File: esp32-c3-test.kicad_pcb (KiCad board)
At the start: 2 copper layers, 40 x 40 mm, 31 parts, among them J1 Conn_01x03, J2 Conn_01x02, J3 Conn_01x01, J4 Conn_01x02, J5 Conn_01x02, J6 Conn_01x02, J9 USB_B_Micro, Q1 DTC143E, Q2 DTC143E, Q3 DTC143E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

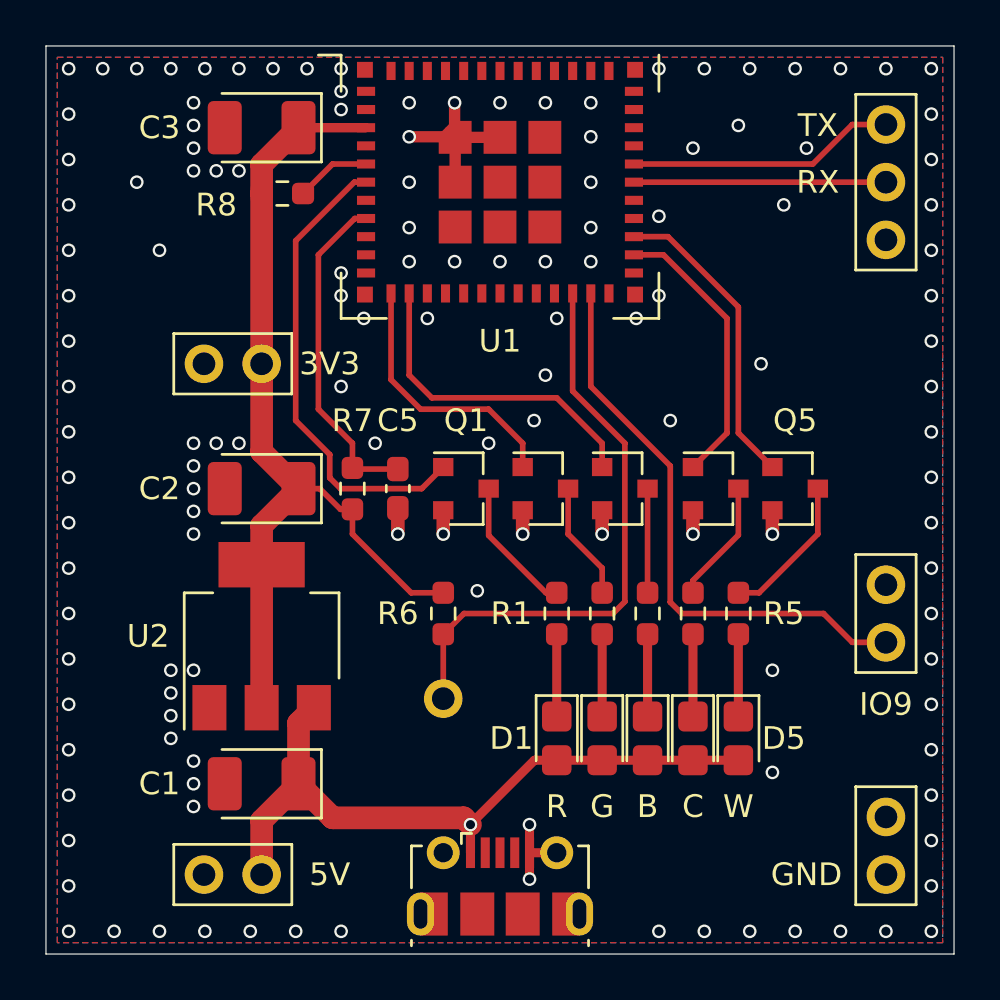
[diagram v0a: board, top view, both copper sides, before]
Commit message: 1. change c5 to c4 2. modify silkscreen of esp32-c3-mini-1 footprint to avoid via 3. move a few vias
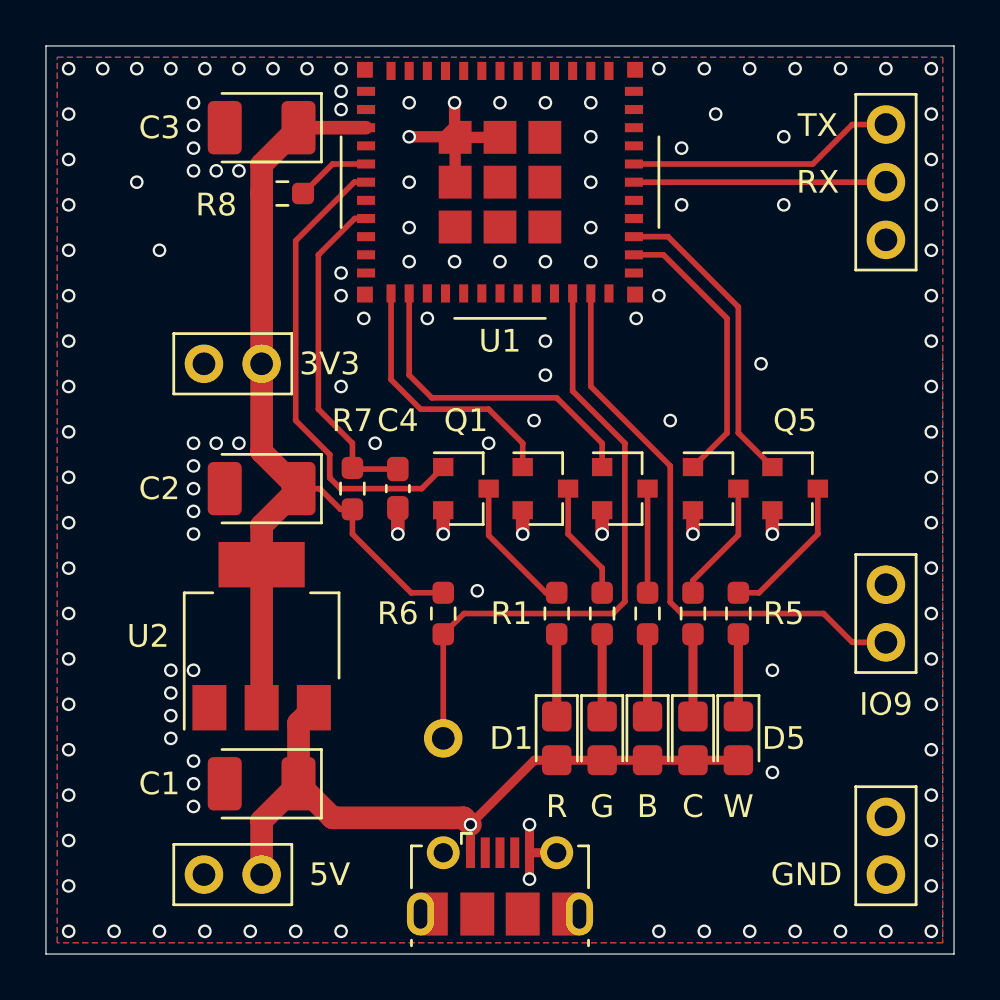
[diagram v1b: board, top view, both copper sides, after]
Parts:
- C1, C2: value CP -> 10u
- moved J3 1.75 mm to (97.5, 85.5)
- renumbered C5 to C4
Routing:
- net /IO8: track 26.0 -> 27.7 mm
